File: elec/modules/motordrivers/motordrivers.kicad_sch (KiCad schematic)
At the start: 16 parts, among them IC2 VNH5019ATR-E, J1 Conn_01x02, J10 Conn_01x05, J2 Conn_01x05, J9 Conn_01x05, Q1 AON6354

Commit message: did motor driver example
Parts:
- added J3: Conn_01x05, Connector_PinHeader_2.54mm:PinHeader_1x05_P2.54mm_Vertical, symbol Connector_Generic:Conn_01x05
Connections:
- net M PWM: now also J9.4 (Pin_4); no longer J9.2 (Pin_2)
- net M SW: now also J9.2 (Pin_2); no longer J9.4 (Pin_4)
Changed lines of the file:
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@@
 	)
 	(label "M PWM"
-		(at 93.98 71.12 0)
+		(at 93.98 66.04 0)
 		(effects
 			(font
@@
 	)
 	(label "M SW"
-		(at 93.98 66.04 0)
+		(at 93.98 71.12 0)
 		(effects
 			(font
@@
 					(unit 1)
 				)
+			)
+		)
+	)
+	(symbol
+		(lib_id "Connector_Generic:Conn_01x05")
+		(at 43.18 86.36 0)
+		(unit 1)
+		(exclude_from_sim no)
+		(in_bom yes)
+		(on_board yes)
+		(dnp no)
+		(fields_autoplaced yes)
+		(property "Reference" "J3"
+			(at 45.72 85.0899 0)
+			(effects
+				(font
+					(size 1.27 1.27)
+				)
+				(justify left)
+			)
+		)
+		(property "Value" "Conn_01x05"
+			(at 45.72 87.6299 0)
+			(effects
+				(font
+					(size 1.27 1.27)
+				)
+				(justify left)
+			)
+		)
+		(property "Footprint" "Connector_PinHeader_2.54mm:PinHeader_1x05_P2.54mm_Vertical"
+			(at 43.18 86.36 0)
+			(effects
+				(font
+					(size 1.27 1.27)
+				)
+				(hide yes)
+			)
+		)
+		(property "Datasheet" "~"
+			(at 43.18 86.36 0)
+			(effects
+				(font
+					(size 1.27 1.27)
+				)
+				(hide yes)
+			)
+		)
+		(property "Description" "Generic connector, single row, 01x05, script generated (kicad-library-utils/schlib/autogen/connector/)"
+			(at 43.18 86.36 0)
+			(effects
+				(font
+					(size 1.27 1.27)
+				)
+				(hide yes)
+			)
+		)
+		(pin "2"
+		)
+		(pin "3"
+		)
+		(pin "4"
+		)
+		(pin "5"
+		)
+		(pin "1"
+		)
+		(instances
+			(project "motordrivers"
+				(path "/878b5707-356f-480c-a2af-3bf932fc4ec2"
+					(reference "J3")
+					(unit 1)
+				)

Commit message: i think thats drivers done
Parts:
- removed J10, J2, J9: Conn_01x05, Pinheaders:PinHeader_1x05_P2.54mm_Vertical, symbol Connector_Generic:Conn_01x05
- removed J3: Conn_01x05, Connector_PinHeader_2.54mm:PinHeader_1x05_P2.54mm_Vertical, symbol Connector_Generic:Conn_01x05
- added J2, J3: Conn_01x08, Pinheaders:PinHeader_1x08_P2.54mm_Vertical, symbol Connector_Generic:Conn_01x08
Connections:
- net +12V: now also J3.1 (Pin_1), J3.2 (Pin_2), J3.3 (Pin_3)
- net +3V3: now also J2.4 (Pin_4), J2.5 (Pin_5)
- net GND: now also J2.1 (Pin_1), J2.8 (Pin_8), J3.6 (Pin_6), J3.7 (Pin_7), J3.8 (Pin_8)
- net M IN A: now also J2.2 (Pin_2)
- net M IN B: now also J2.7 (Pin_7)
- net M PWM: now also J2.6 (Pin_6)
- net M SW: now also J2.3 (Pin_3)
- no-connect marks 2 -> 4

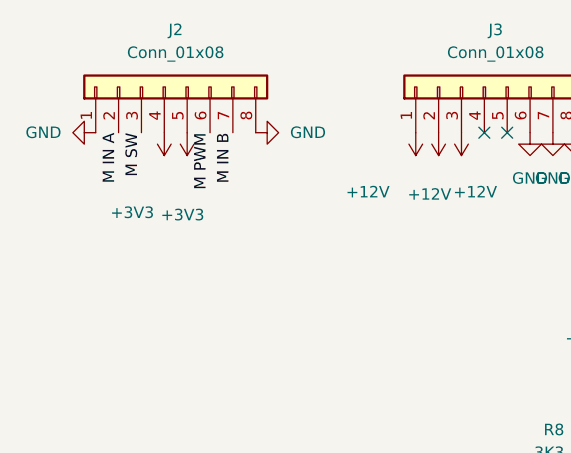
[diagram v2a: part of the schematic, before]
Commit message: aligned pogos
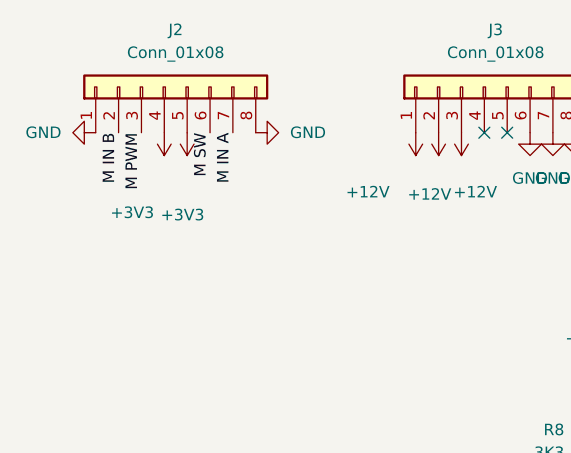
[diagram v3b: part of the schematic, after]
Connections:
- net M IN A: now also J2.7 (Pin_7); no longer J2.2 (Pin_2)
- net M IN B: now also J2.2 (Pin_2); no longer J2.7 (Pin_7)
- net M PWM: now also J2.3 (Pin_3); no longer J2.6 (Pin_6)
- net M SW: now also J2.6 (Pin_6); no longer J2.3 (Pin_3)
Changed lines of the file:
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@@
 	)
 	(label "M IN A"
-		(at 82.55 45.72 270)
+		(at 95.25 45.72 270)
 		(effects
 			(font
@@
 	)
 	(label "M PWM"
-		(at 92.71 45.72 270)
+		(at 85.09 45.72 270)
 		(effects
 			(font
@@
 	)
 	(label "M IN B"
-		(at 95.25 45.72 270)
+		(at 82.55 45.72 270)
 		(effects
 			(font
@@
 	)
 	(label "M SW"
-		(at 85.09 45.72 270)
+		(at 92.71 45.72 270)
 		(effects
 			(font

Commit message: motor drivers completed
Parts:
- C15: footprint drivers:CP_Radial_D8.0mm_P3.50mm -> Capacitor_THT:CP_Radial_D8.0mm_P3.50mm
- C16: footprint drivers:cap0603 -> footprints:Capacitor_0603
- R10, R11, R12, R13, R14, R15, R8, R9: footprint drivers:res0603 -> footprints:Resistor_0603
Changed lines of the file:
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@@
 			)
 		)
-		(property "Footprint" "drivers:res0603"
+		(property "Footprint" "footprints:Resistor_0603"
 			(at 141.478 80.01 90)
 			(effects
@@
 			)
 		)
-		(property "Footprint" "drivers:cap0603"
+		(property "Footprint" "footprints:Capacitor_0603"
 			(at 202.2348 111.76 0)
 			(effects
@@
 			)
 		)
-		(property "Footprint" "drivers:res0603"
+		(property "Footprint" "footprints:Resistor_0603"
 			(at 135.382 110.49 90)
 			(effects
@@
 			)
 		)
-		(property "Footprint" "drivers:res0603"
+		(property "Footprint" "footprints:Resistor_0603"
 			(at 146.05 91.948 90)
 			(effects
@@
 			)
 		)
-		(property "Footprint" "drivers:res0603"
+		(property "Footprint" "footprints:Resistor_0603"
 			(at 146.05 97.028 90)
 			(effects
@@
 			)
 		)
-		(property "Footprint" "drivers:res0603"
+		(property "Footprint" "footprints:Resistor_0603"
 			(at 146.05 102.362 90)
 			(effects
@@
 			)
 		)
-		(property "Footprint" "drivers:res0603"
+		(property "Footprint" "footprints:Resistor_0603"
 			(at 146.05 88.138 90)
 			(effects
@@
 			)
 		)
-		(property "Footprint" "drivers:res0603"
+		(property "Footprint" "footprints:Resistor_0603"
 			(at 146.05 97.282 90)
 			(effects
@@
 			)
 		)
-		(property "Footprint" "drivers:CP_Radial_D8.0mm_P3.50mm"
+		(property "Footprint" "Capacitor_THT:CP_Radial_D8.0mm_P3.50mm"
 			(at 191.4652 111.76 0)
 			(effects
@@
 			)
 		)
-		(property "Footprint" "drivers:res0603"
+		(property "Footprint" "footprints:Resistor_0603"
 			(at 132.842 80.01 90)
 			(effects
